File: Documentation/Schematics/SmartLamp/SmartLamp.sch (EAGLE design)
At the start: 51 parts, among them J1 POWER_JACKPTH_BREAD, Q1 STN4NF03L, Q2 STN4NF03L, Q3 STN4NF03L, Q4 FA-128, Q5 MC-306, U1 TPS71530, U2 DS3231MZ, U3 CC2541_RHA_40

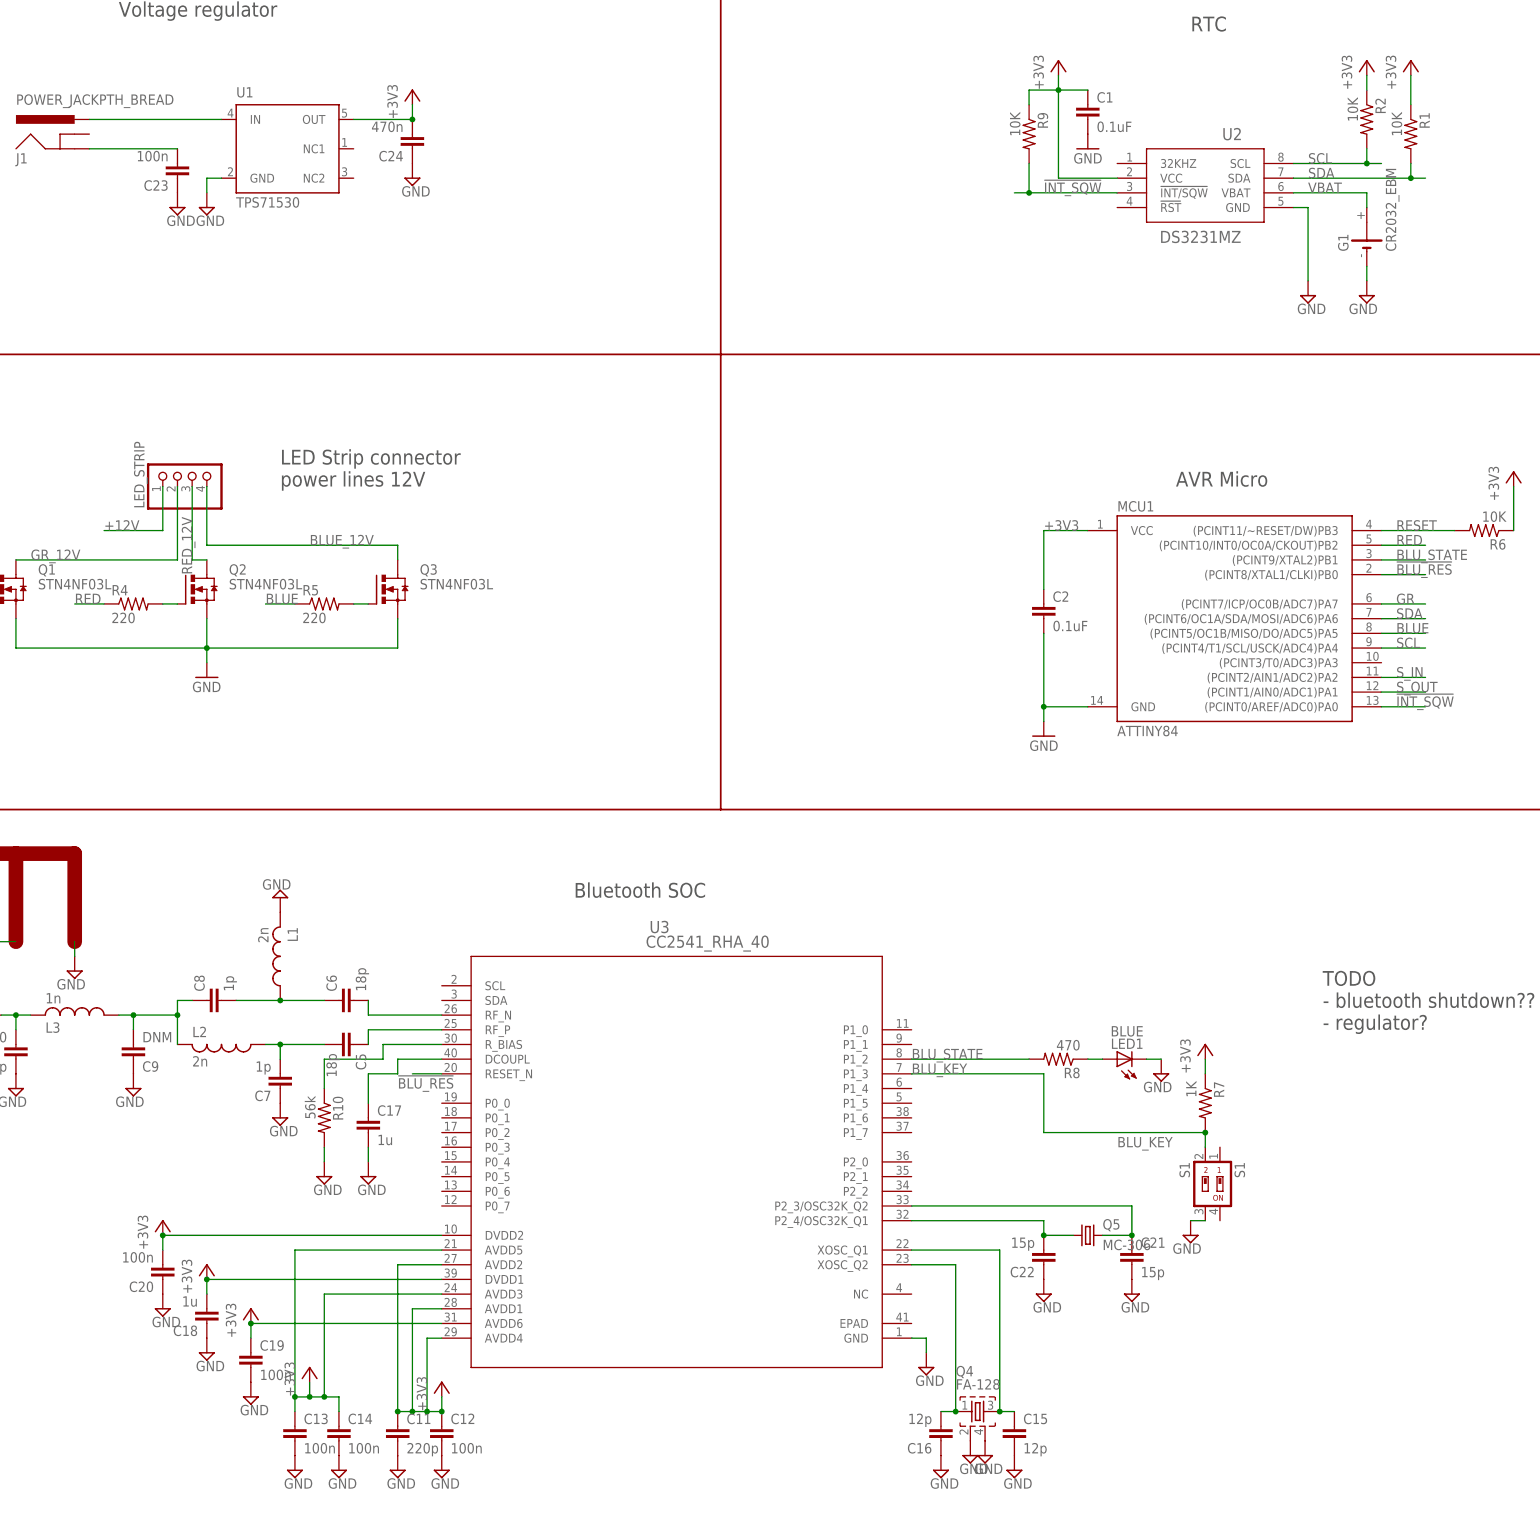
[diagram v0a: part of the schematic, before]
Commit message: New device for CC2514, first routed version of the board. Still clearence problem on the device!
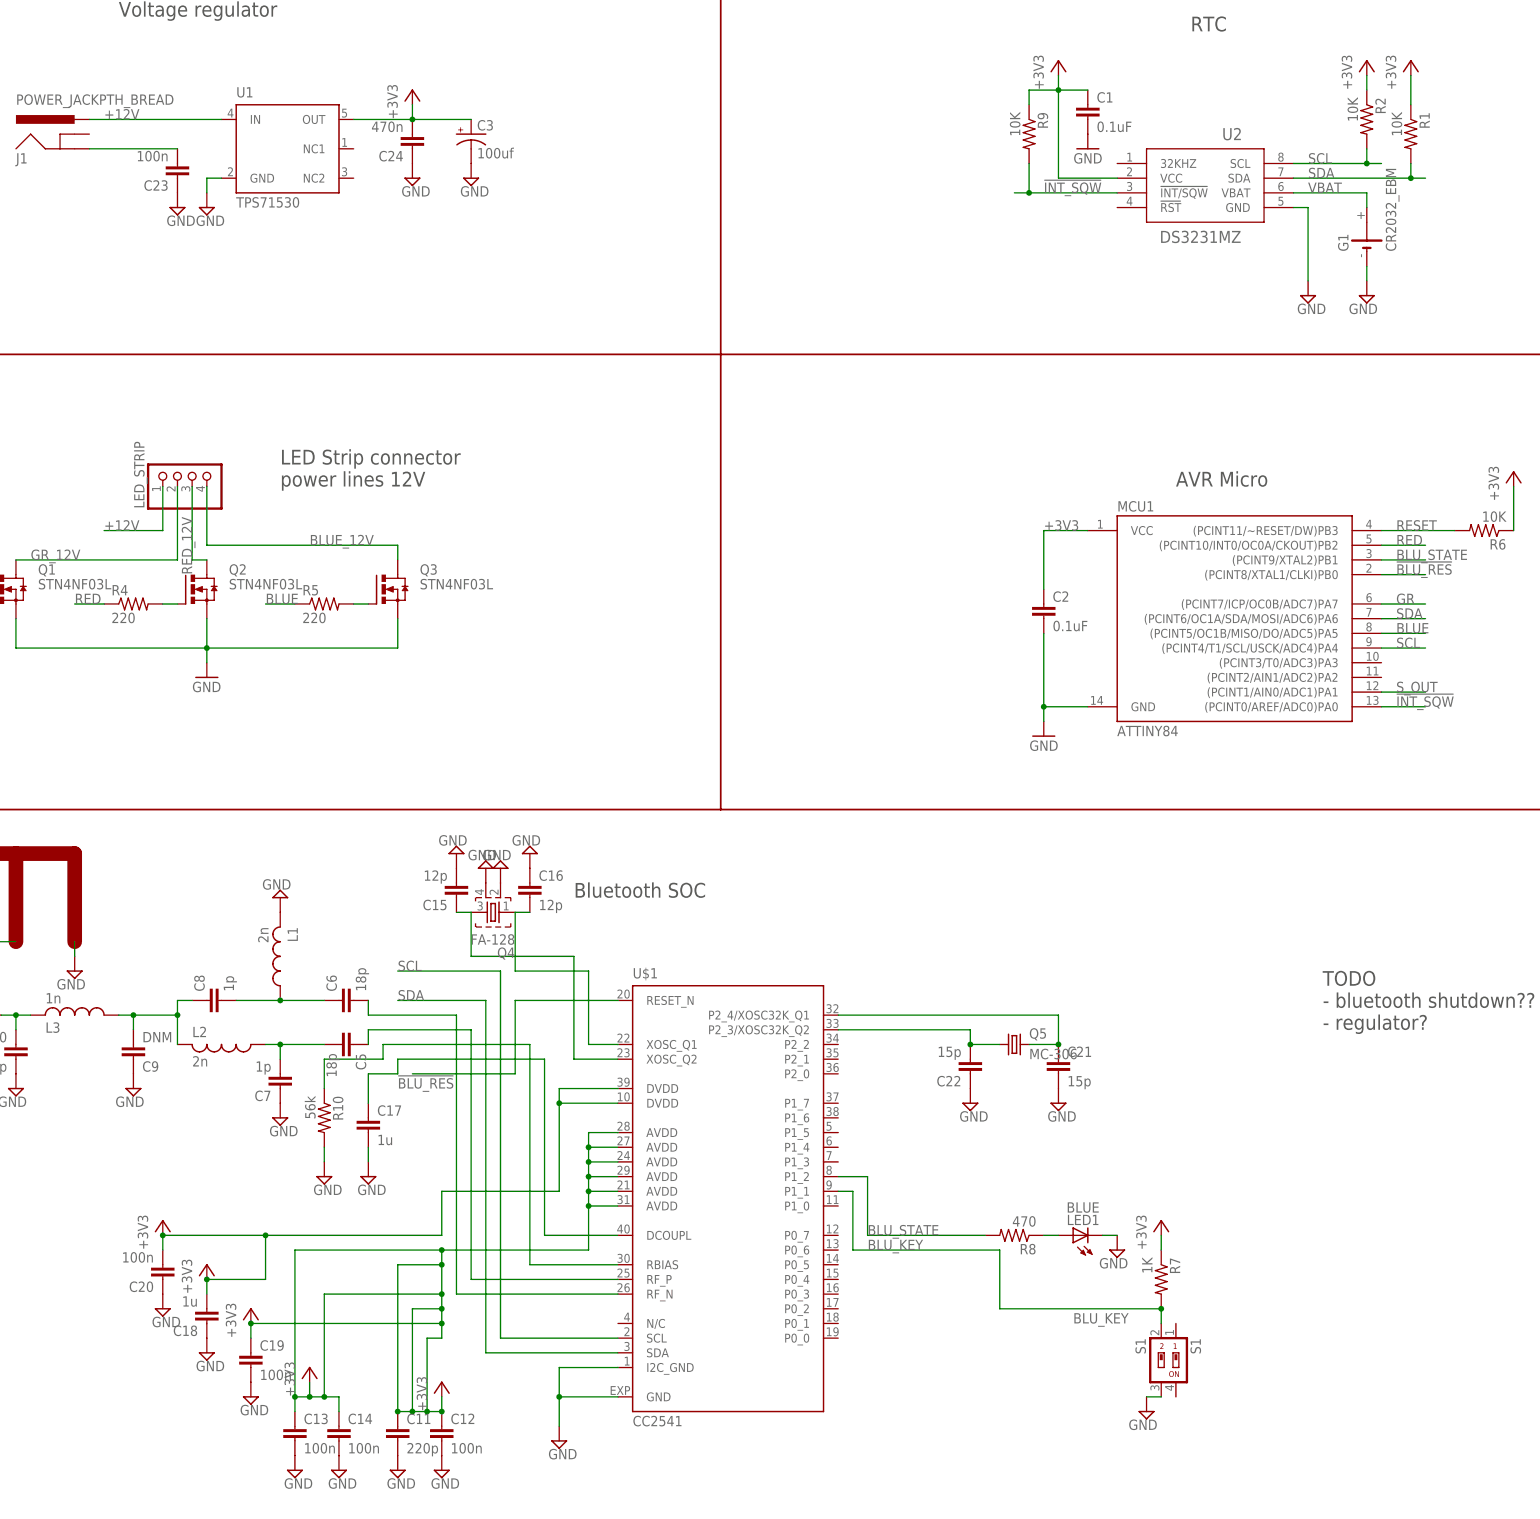
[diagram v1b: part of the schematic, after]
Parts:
- removed U3: CC2541_RHA_40, CC254X_Texas:CC2541_RHA_40
- added C3: 100uf, SparkFun-Capacitors:CAP_POLC
- added U$1: CC2541, ST-CC254X:CC2541
- R9: device rcl:R-US_R1206 -> rcl:R-US_R0805
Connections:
- removed net N$14: C16.2, Q4.1, U3.XOSC_Q2
- removed net N$15: C15.1, Q4.3, U3.XOSC_Q1
- removed net S_IN: MCU1.(PCINT2/AIN1/ADC2)PA2
- removed net VDD: C11.1, C12.1, C19.1, C24.2, U1.OUT, U3.AVDD1, U3.AVDD2, U3.AVDD4, U3.AVDD6
- new net N$1: C16.2, Q4.1, U$1.XOSC_Q1
- new net N$3: C15.1, Q4.3, U$1.XOSC_Q2
- net !BLU_RES: now also U$1.RESET_N; no longer U3.RESET_N
- net +3V3: now also C11.1, C12.1, C19.1, C24.2, C3.+, U$1.AVDD@1, U$1.AVDD@2, U$1.AVDD@3, U$1.AVDD@4, U$1.AVDD@5, U$1.AVDD@6, U$1.DVDD@1, U$1.DVDD@2, U1.OUT; no longer U3.AVDD3, U3.AVDD5, U3.DVDD1, U3.DVDD2
- net BLU_KEY: now also U$1.P1_1; no longer U3.P1_3
- net BLU_STATE: now also U$1.P1_2; no longer U3.P1_2
- net GND: now also C3.-, U$1.GND, U$1.I2C_GND; no longer U3.GND
- net N$13: now also U$1.RBIAS; no longer U3.R_BIAS
- net N$16: now also U$1.DCOUPL; no longer U3.DCOUPL
- net N$17: now also U$1.P2_3/XOSC32K_Q2; no longer U3.P2_4/OSC32K_Q1
- net N$18: now also U$1.P2_4/XOSC32K_Q1; no longer U3.P2_3/OSC32K_Q2
- net N$2: now also U$1.RF_N; no longer U3.RF_N
- net N$9: now also U$1.RF_P; no longer U3.RF_P
- net SCL: now also U$1.SCL
- net SDA: now also U$1.SDA
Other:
- moved on the sheet: C15, C16, C21, C22, LED1, Q4, Q5, R7, R8, S1

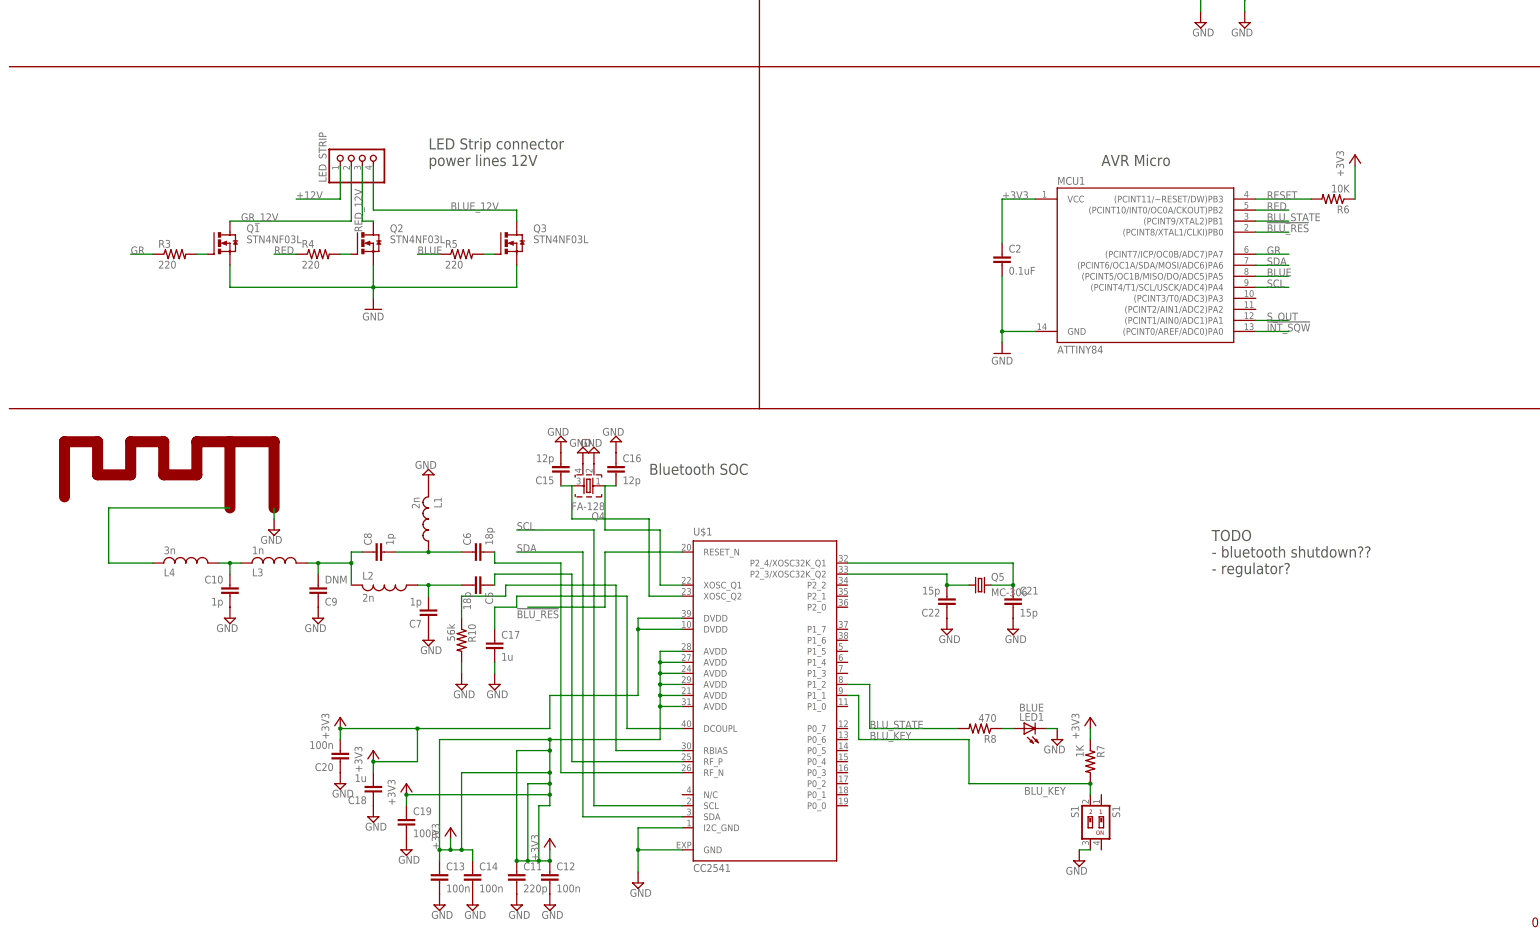
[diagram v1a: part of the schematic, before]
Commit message: Routing of the board in progress.. new version with ATMega168/328P
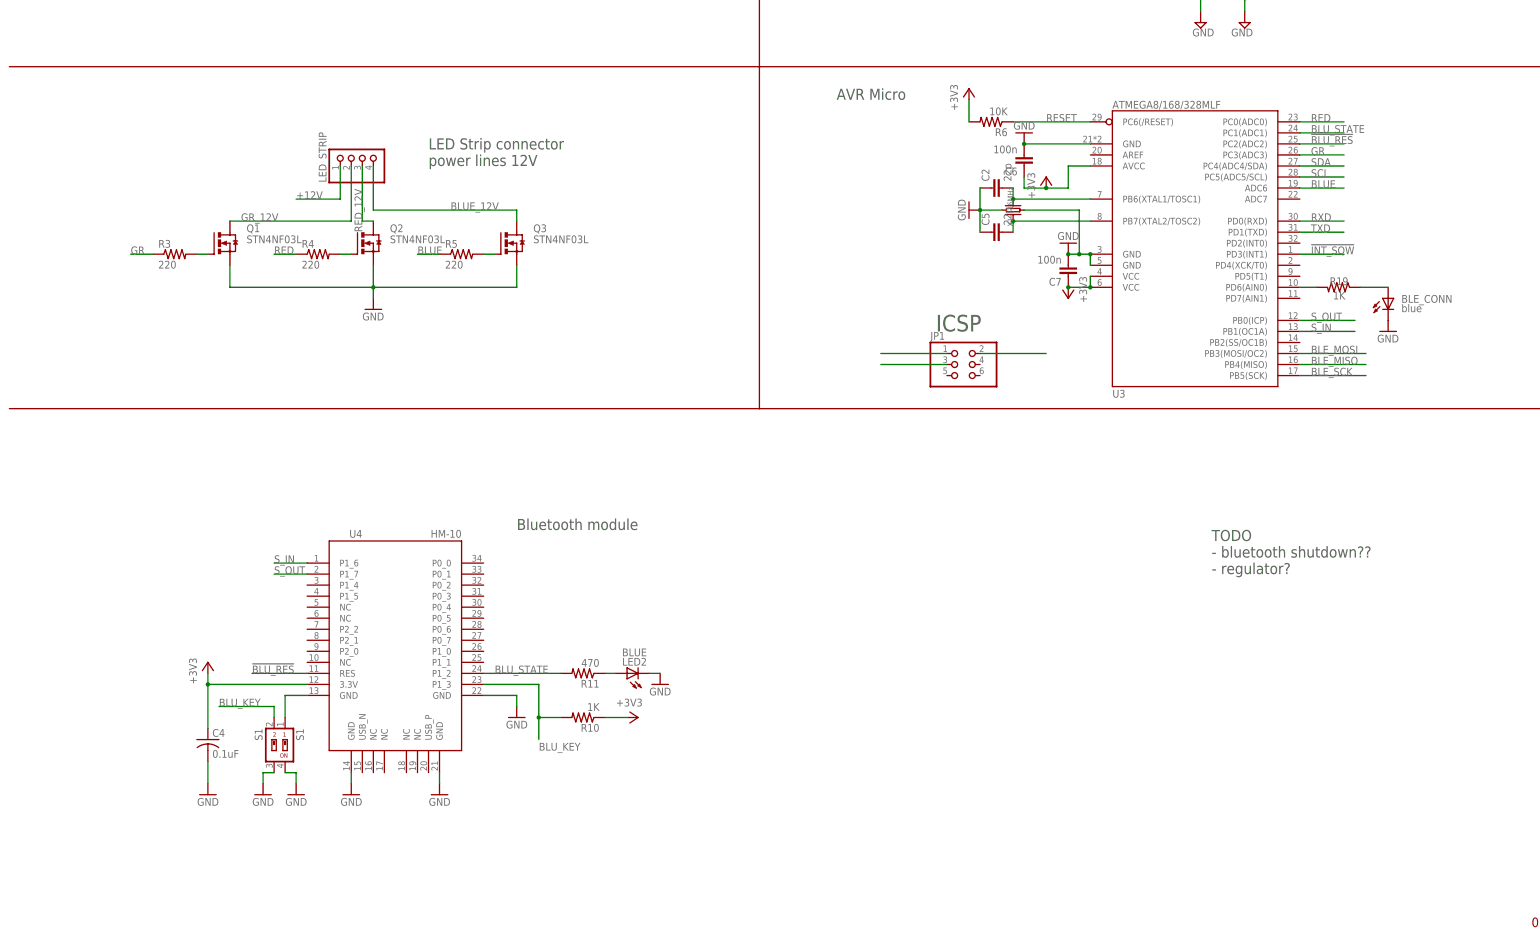
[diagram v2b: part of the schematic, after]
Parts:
- removed A1: TI_2.4GHZ_MIFALEFT, antennas:TI_2.4GHZ_MIFALEFT
- removed C10, C8: 1p, resistor:C-EUC0805
- removed C11: 220p, resistor:C-EUC0805
- removed C12, C13, C14, C19, C20: 100n, resistor:C-EUC0805
- removed C15, C16: 12p, resistor:C-EUC0805
- removed C17, C18: 1u, resistor:C-EUC0805
- removed C21, C22: 15p, resistor:C-EUC0805
- removed C9: DNM, resistor:C-EUC0805
- removed L1, L2: 2n, rcl:L-USL3225P
- removed L3: 1n, rcl:L-USL3225P
- removed L4: 3n, rcl:L-USL3225P
- removed LED1: BLUE, adafruit:LEDCHIPLED_1206
- removed MCU1: ATTINY84, SparkFun-IC-Microcontroller:ATTINY84
- removed Q4: FA-128, crystal:FA-128
- removed Q5: MC-306, crystal:MC-306
- removed R7: 1K, rcl:R-US_R0805
- removed R8: 470, rcl:R-US_R0805
- removed U$1: CC2541, ST-CC254X:CC2541
- added BLE_CONN: blue, adafruit:LEDCHIP-LED0805
- added C4: 0.1uF, adafruit:C-USC0805
- added JP1: (no value), pinhead:PINHD-2X3
- added LED2: BLUE, adafruit:LEDCHIP-LED0805
- added R11: 470, rcl:R-US_R0805
- added R19: 1K, rcl:R-US_R0805
- added U3: ATMEGA8/168/328MLF, IC:ATMEGA8/168/328MLF
- added U4: HM-10, HM-10_BLE:HM-10
- added X1: 16MHz, Discrete:CRYSTAL'3225'
- C2: value 0.1uF -> 22p
- C5: value 18p -> 22p; device resistor:C-EUC0805 -> rcl:C-EUC0805
- C6: value 18p -> 100n; device resistor:C-EUC0805 -> rcl:C-EUC0805
- C7: value 1p -> 100n; device resistor:C-EUC0805 -> rcl:C-EUC0805
- R10: value 56k -> 1K
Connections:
- net N$4 renamed 12V_GND
- removed net N$10: LED1.A, R8.1
- removed net N$12: C5.2, C7.2, L2.1
- removed net N$13: R10.1, U$1.RBIAS
- removed net N$16: C17.1, U$1.DCOUPL
- removed net N$17: C22.2, Q5.1, U$1.P2_3/XOSC32K_Q2
- removed net N$18: C21.1, Q5.2, U$1.P2_4/XOSC32K_Q1
- removed net N$19: C10.1, L3.2, L4.1
- removed net N$2: C6.2, U$1.RF_N
- removed net N$20: C8.1, C9.2, L2.2, L3.1
- removed net N$3: C15.1, Q4.3, U$1.XOSC_Q2
- removed net N$44: A1.FEED, L4.2
- removed net N$5: C6.1, C8.2, L1.1
- removed net N$9: C5.1, U$1.RF_P
- new net BLE_MISO: JP1.1, U3.PB4(MISO)
- new net BLE_MOSI: JP1.2, U3.PB3(MOSI/OC2)
- new net BLE_SCK: JP1.3, U3.PB5(SCK)
- new net BLU_SWITCH: S1.1, U4.GND@1
- new net N$15: C2.2, U3.PB6(XTAL1/TOSC1), X1.2
- new net N$21: C5.2, U3.PB7(XTAL2/TOSC2), X1.1
- new net N$22: R19.2, U3.PD6(AIN0)
- new net N$23: BLE_CONN.A, R19.1
- new net RXD: U3.PD0(RXD)
- new net S_IN: U3.PB1(OC1A), U4.P1_6
- new net TXD: U3.PD1(TXD)
- net !BLU_RES: now also U3.PC2(ADC2), U4.RES; no longer MCU1.(PCINT8/XTAL1/CLKI)PB0, U$1.RESET_N
- net !INT_SQW: now also U3.PD3(INT1); no longer MCU1.(PCINT0/AREF/ADC0)PA0
- net +3V3: now also C4.1, C6.1, C7.1, R10.1, R6.2, U3.AVCC, U3.VCC@1, U3.VCC@2, U4.3.3V; no longer C11.1, C12.1, C13.1, C14.1, C18.2, C19.1, C2.1, C20.2, MCU1.VCC, R6.1, R7.1, U$1.AVDD@1, U$1.AVDD@2, U$1.AVDD@3, U$1.AVDD@4, U$1.AVDD@5, U$1.AVDD@6, U$1.DVDD@1, U$1.DVDD@2
- net BLUE: now also U3.ADC6; no longer MCU1.(PCINT5/OC1B/MISO/DO/ADC5)PA5
- net BLU_KEY: now also R10.2, U4.P1_3; no longer R7.2, U$1.P1_1
- net BLU_STATE: now also R11.2, U3.PC1(ADC1), U4.P1_2; no longer MCU1.(PCINT9/XTAL2)PB1, R8.2, U$1.P1_2
- net GND: now also BLE_CONN.C, C2.1, C4.2, C5.1, C6.2, C7.2, LED2.C, S1.4, U3.GND, U3.GND@1, U3.GND@2, U4.GND@2, U4.GND@3, U4.GND@4, X1.GND_BOTTOM, X1.GND_TOP; no longer A1.GND, C10.2, C11.2, C12.2, C13.2, C14.2, C15.2, C16.1, C17.2, C18.1, C19.2, C2.2, C20.1, C21.2, C22.1, C7.1, C9.1, L1.2, LED1.C, MCU1.GND, Q4.2, Q4.4, R10.2, U$1.GND, U$1.I2C_GND
- net GR: now also U3.PC3(ADC3); no longer MCU1.(PCINT7/ICP/OC0B/ADC7)PA7
- net N$1: now also LED2.A, R11.1; no longer C16.2, Q4.1, U$1.XOSC_Q1
- net RED: now also U3.PC0(ADC0); no longer MCU1.(PCINT10/INT0/OC0A/CKOUT)PB2
- net RESET: now also R6.1, U3.PC6(/RESET); no longer MCU1.(PCINT11/~RESET/DW)PB3, R6.2
- net SCL: now also U3.PC5(ADC5/SCL); no longer MCU1.(PCINT4/T1/SCL/USCK/ADC4)PA4, U$1.SCL
- net SDA: now also U3.PC4(ADC4/SDA); no longer MCU1.(PCINT6/OC1A/SDA/MOSI/ADC6)PA6, U$1.SDA
- net S_OUT: now also U3.PB0(ICP), U4.P1_7; no longer MCU1.(PCINT1/AIN0/ADC1)PA1
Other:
- note added: "Bluetooth module"
- note added: "ICSP"
- note removed: "Bluetooth SOC"
- moved on the sheet: C2, C5, C6, C7, R10, R6, S1

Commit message: Routing completed, added gerber files, fixed ICSP connection
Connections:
- net BLE_MISO renamed MISO
- net BLE_SCK renamed SCK
- removed net 12V_GND: C23.2, J1.GND
- removed net BLE_MOSI: JP1.2, U3.PB3(MOSI/OC2)
- removed net RXD: U3.PD0(RXD)
- removed net TXD: U3.PD1(TXD)
- new net MOSI: JP1.4, U3.PB3(MOSI/OC2)
- net +12V: now also C23.2
- net +3V3: now also JP1.2
- net GND: now also J1.GND, JP1.6
- net RESET: now also JP1.5
- net S_IN: now also U3.PD1(TXD); no longer U3.PB1(OC1A)
- net S_OUT: now also U3.PD0(RXD); no longer U3.PB0(ICP)
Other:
- moved on the sheet: BLE_CONN, C1, C2, C23, C24, C3, C4, C5, C6, C7, G1, J1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
